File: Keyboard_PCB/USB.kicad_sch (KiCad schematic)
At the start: 3 parts, among them J6 CH_USB_C, U6 USBLC6-2SC6

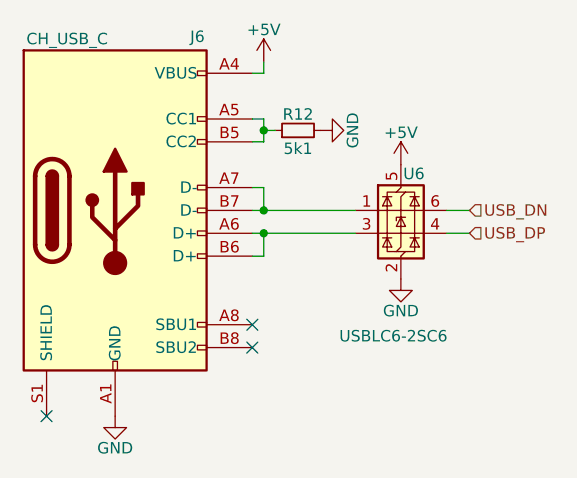
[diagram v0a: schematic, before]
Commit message: STM32U385 pin assignment progress
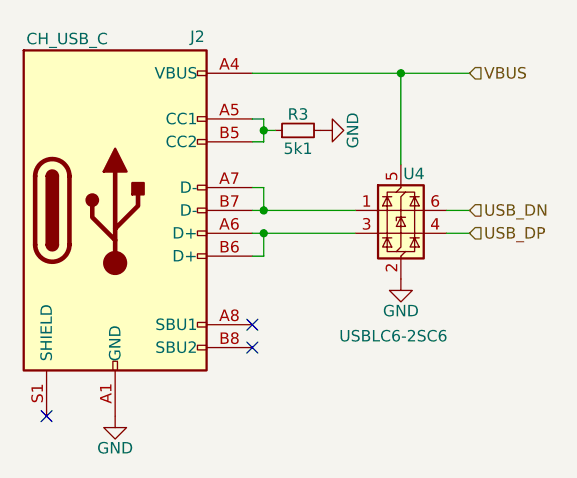
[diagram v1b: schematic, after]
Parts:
- renumbered J6 to J2, R12 to R3, U6 to U4
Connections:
- net +5V renamed VBUS
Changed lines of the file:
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@@
+	)
+	(junction
+		(at 93.98 48.26)
+		(diameter 0)
+		(color 0 0 0 0)
 	)
 	(junction
@@
 	(wire
 		(pts
+			(xy 101.6 48.26) (xy 93.98 48.26)
+		)
+		(stroke
+			(width 0)
+			(type default)
+		)
+	)
+	(wire
+		(pts
 			(xy 78.74 63.5) (xy 77.47 63.5)
 		)
@@
 	(wire
 		(pts
-			(xy 77.47 48.26) (xy 78.74 48.26)
+			(xy 77.47 48.26) (xy 93.98 48.26)
 		)
 		(stroke
@@
 	(wire
 		(pts
-			(xy 78.74 46.99) (xy 78.74 48.26)
-		)
-		(stroke
-			(width 0)
-			(type default)
-		)
-	)
-	(wire
-		(pts
 			(xy 77.47 66.04) (xy 78.74 66.04)
 		)
@@
 		(pts
 			(xy 78.74 66.04) (xy 88.9 66.04)
+		)
+		(stroke
+			(width 0)
+			(type default)
+		)
+	)
+	(wire
+		(pts
+			(xy 93.98 48.26) (xy 93.98 58.42)
 		)
 		(stroke
@@
 		(shape input)
 		(at 101.6 66.04 0)
+		(effects
+			(font
+				(size 1.27 1.27)
+			)
+			(justify left)
+		)
+	)
+	(hierarchical_label "VBUS"
+		(shape input)
+		(at 101.6 48.26 0)
 		(effects
 			(font
@@
 		(on_board yes)
 		(dnp no)
-		(property "Reference" "U6"
+		(property "Reference" "U4"
 			(at 94.234 59.436 0)
 			(effects
@@
 			(project "RF_HID_module_test"
 				(path "/dd51e792-c76c-4d43-96de-494177f3b593/99a36190-5dce-43c5-9e98-275e559646eb"
-					(reference "U6")
+					(reference "U4")
 					(unit 1)
 				)
@@
 		(on_board yes)
 		(dnp no)
-		(property "Reference" "R12"
+		(property "Reference" "R3"
 			(at 82.55 52.832 90)
 			(effects
@@
 			(project ""
 				(path "/dd51e792-c76c-4d43-96de-494177f3b593/99a36190-5dce-43c5-9e98-275e559646eb"
-					(reference "R12")
+					(reference "R3")
 					(unit 1)
 				)
@@
 		(on_board yes)
 		(dnp no)
-		(property "Reference" "#PWR047"
+		(property "Reference" "#PWR014"
 			(at 93.98 77.47 0)
 			(effects
@@
 			(project "RF_HID_module_test"
 				(path "/dd51e792-c76c-4d43-96de-494177f3b593/99a36190-5dce-43c5-9e98-275e559646eb"
-					(reference "#PWR047")
+					(reference "#PWR014")
 					(unit 1)
 				)
@@
 		(on_board yes)
 		(dnp no)
-		(property "Reference" "#PWR045"
+		(property "Reference" "#PWR013"
 			(at 91.44 54.61 0)
 			(effects
@@
 			(project "RF_HID_module_test"
 				(path "/dd51e792-c76c-4d43-96de-494177f3b593/99a36190-5dce-43c5-9e98-275e559646eb"
-					(reference "#PWR045")
-					(unit 1)
-				)
-			)
-		)
-	)
-	(symbol
-		(lib_id "power:+5V")
-		(at 78.74 46.99 0)
-		(unit 1)
-		(exclude_from_sim no)
-		(in_bom yes)
-		(on_board yes)
-		(dnp no)
-		(property "Reference" "#PWR044"
-			(at 78.74 50.8 0)
-			(effects
-				(font
-					(size 1.27 1.27)
-				)
-				(hide yes)
-			)
-		)
-		(property "Value" "+5V"
-			(at 78.74 43.434 0)
-			(effects
-				(font
-					(size 1.27 1.27)
-				)
-			)
-		)
-		(property "Footprint" ""
-			(at 78.74 46.99 0)
-			(effects
-				(font
-					(size 1.27 1.27)
-				)
-				(hide yes)
-			)
-		)
-		(property "Datasheet" ""
-			(at 78.74 46.99 0)
-			(effects
-				(font
-					(size 1.27 1.27)
-				)
-				(hide yes)
-			)
-		)
-		(property "Description" "Power symbol creates a global label with name \"+5V\""
-			(at 78.74 46.99 0)
-			(effects
-				(font
-					(size 1.27 1.27)
-				)
-				(hide yes)
-			)
-		)
-		(pin "1"
-		)
-		(instances
-			(project "RF_HID_module_test"
-				(path "/32b1f824-104d-4f37-b265-1c31215c2fe4/3052776d-f0df-4f5c-b23a-46f73ae78b94"
-					(reference "#PWR044")
-					(unit 1)
-				)
-				(path "/32b1f824-104d-4f37-b265-1c31215c2fe4/35fb170e-cc4d-4774-8b9f-87fa9e2bb590"
-					(reference "#PWR049")
-					(unit 1)
-				)
-			)
-			(project "RF_HID_module_test"
-				(path "/dd51e792-c76c-4d43-96de-494177f3b593/99a36190-5dce-43c5-9e98-275e559646eb"
-					(reference "#PWR044")
+					(reference "#PWR013")
 					(unit 1)
 				)
@@
 		(on_board yes)
 		(dnp no)
-		(property "Reference" "#PWR048"
+		(property "Reference" "#PWR015"
 			(at 62.23 92.71 0)
 			(effects
@@
 			(project "RF_HID_module_test"
 				(path "/dd51e792-c76c-4d43-96de-494177f3b593/99a36190-5dce-43c5-9e98-275e559646eb"
-					(reference "#PWR048")
-					(unit 1)
-				)
-			)
-		)
-	)
-	(symbol
-		(lib_id "power:+5V")
-		(at 93.98 58.42 0)
-		(unit 1)
-		(exclude_from_sim no)
-		(in_bom yes)
-		(on_board yes)
-		(dnp no)
-		(property "Reference" "#PWR046"
-			(at 93.98 62.23 0)
-			(effects
-				(font
-					(size 1.27 1.27)
-				)
-				(hide yes)
-			)
-		)
-		(property "Value" "+5V"
-			(at 93.98 54.864 0)
-			(effects
-				(font
-					(size 1.27 1.27)
-				)
-			)
-		)
-		(property "Footprint" ""
-			(at 93.98 58.42 0)
-			(effects
-				(font
-					(size 1.27 1.27)
-				)
-				(hide yes)
-			)
-		)
-		(property "Datasheet" ""
-			(at 93.98 58.42 0)
-			(effects
-				(font
-					(size 1.27 1.27)
-				)
-				(hide yes)
-			)
-		)
-		(property "Description" "Power symbol creates a global label with name \"+5V\""
-			(at 93.98 58.42 0)
-			(effects
-				(font
-					(size 1.27 1.27)
-				)
-				(hide yes)
-			)
-		)
-		(pin "1"
-		)
-		(instances
-			(project "RF_HID_module_test"
-				(path "/32b1f824-104d-4f37-b265-1c31215c2fe4/3052776d-f0df-4f5c-b23a-46f73ae78b94"
-					(reference "#PWR046")
-					(unit 1)
-				)
-				(path "/32b1f824-104d-4f37-b265-1c31215c2fe4/35fb170e-cc4d-4774-8b9f-87fa9e2bb590"
-					(reference "#PWR051")
-					(unit 1)
-				)
-			)
-			(project "RF_HID_module_test"
-				(path "/dd51e792-c76c-4d43-96de-494177f3b593/99a36190-5dce-43c5-9e98-275e559646eb"
-					(reference "#PWR046")
+					(reference "#PWR015")
 					(unit 1)
 				)
@@
 		(on_board yes)
 		(dnp no)
-		(property "Reference" "J6"
+		(property "Reference" "J2"
 			(at 71.374 44.196 0)
 			(effects
@@
 			(project "RF_HID_module_test"
 				(path "/dd51e792-c76c-4d43-96de-494177f3b593/99a36190-5dce-43c5-9e98-275e559646eb"
-					(reference "J6")
-					(unit 1)
-				)
+					(reference "J2")
+					(unit 1)
+				)

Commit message: Schematic done
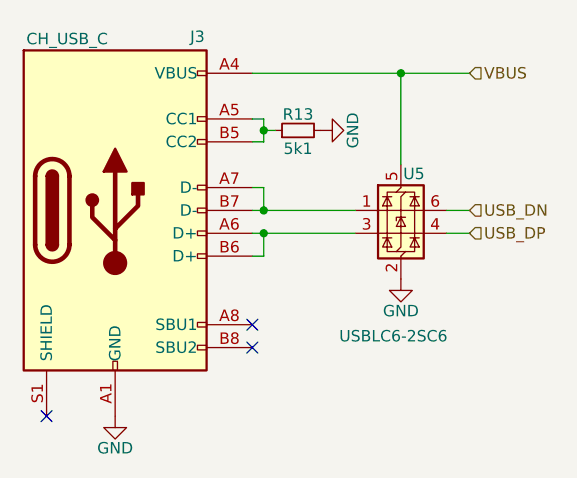
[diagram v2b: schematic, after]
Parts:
- renumbered J2 to J3, R3 to R13, U4 to U5
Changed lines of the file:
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@@
 		(on_board yes)
 		(dnp no)
-		(property "Reference" "U4"
+		(property "Reference" "U5"
 			(at 94.234 59.436 0)
 			(effects
@@
 			(project "RF_HID_module_test"
 				(path "/dd51e792-c76c-4d43-96de-494177f3b593/99a36190-5dce-43c5-9e98-275e559646eb"
-					(reference "U4")
+					(reference "U5")
 					(unit 1)
 				)
@@
 		(on_board yes)
 		(dnp no)
-		(property "Reference" "R3"
+		(property "Reference" "R13"
 			(at 82.55 52.832 90)
 			(effects
@@
 			(project ""
 				(path "/dd51e792-c76c-4d43-96de-494177f3b593/99a36190-5dce-43c5-9e98-275e559646eb"
-					(reference "R3")
+					(reference "R13")
 					(unit 1)
 				)
@@
 		(on_board yes)
 		(dnp no)
-		(property "Reference" "#PWR014"
+		(property "Reference" "#PWR059"
 			(at 93.98 77.47 0)
 			(effects
@@
 			(project "RF_HID_module_test"
 				(path "/dd51e792-c76c-4d43-96de-494177f3b593/99a36190-5dce-43c5-9e98-275e559646eb"
-					(reference "#PWR014")
+					(reference "#PWR059")
 					(unit 1)
 				)
@@
 		(on_board yes)
 		(dnp no)
-		(property "Reference" "#PWR013"
+		(property "Reference" "#PWR058"
 			(at 91.44 54.61 0)
 			(effects
@@
 			(project "RF_HID_module_test"
 				(path "/dd51e792-c76c-4d43-96de-494177f3b593/99a36190-5dce-43c5-9e98-275e559646eb"
-					(reference "#PWR013")
+					(reference "#PWR058")
 					(unit 1)
 				)
@@
 		(on_board yes)
 		(dnp no)
-		(property "Reference" "#PWR015"
+		(property "Reference" "#PWR060"
 			(at 62.23 92.71 0)
 			(effects
@@
 			(project "RF_HID_module_test"
 				(path "/dd51e792-c76c-4d43-96de-494177f3b593/99a36190-5dce-43c5-9e98-275e559646eb"
-					(reference "#PWR015")
+					(reference "#PWR060")
 					(unit 1)
 				)
@@
 		(on_board yes)
 		(dnp no)
-		(property "Reference" "J2"
+		(property "Reference" "J3"
 			(at 71.374 44.196 0)
 			(effects
@@
 			(project "RF_HID_module_test"
 				(path "/dd51e792-c76c-4d43-96de-494177f3b593/99a36190-5dce-43c5-9e98-275e559646eb"
-					(reference "J2")
-					(unit 1)
-				)
+					(reference "J3")
+					(unit 1)
+				)

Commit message: eMMC routing and STM passives
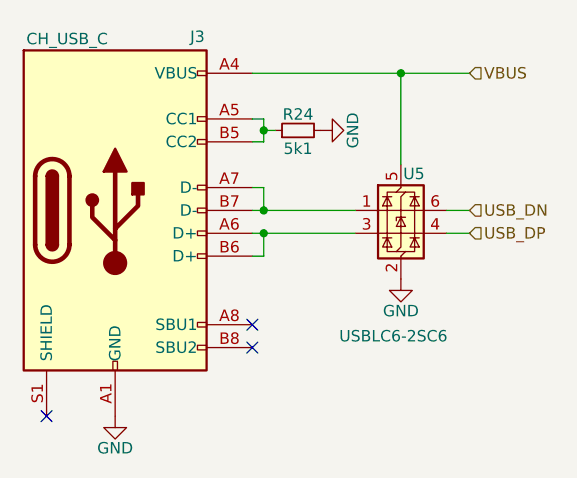
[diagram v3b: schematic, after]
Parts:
- renumbered R13 to R24
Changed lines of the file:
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@@
 		(on_board yes)
 		(dnp no)
-		(property "Reference" "R13"
+		(property "Reference" "R24"
 			(at 82.55 52.832 90)
 			(effects
@@
 			(project ""
 				(path "/dd51e792-c76c-4d43-96de-494177f3b593/99a36190-5dce-43c5-9e98-275e559646eb"
-					(reference "R13")
+					(reference "R24")
 					(unit 1)
 				)
@@
 		(on_board yes)
 		(dnp no)
-		(property "Reference" "#PWR059"
+		(property "Reference" "#PWR072"
 			(at 93.98 77.47 0)
 			(effects
@@
 			(project "RF_HID_module_test"
 				(path "/dd51e792-c76c-4d43-96de-494177f3b593/99a36190-5dce-43c5-9e98-275e559646eb"
-					(reference "#PWR059")
+					(reference "#PWR072")
 					(unit 1)
 				)
@@
 		(on_board yes)
 		(dnp no)
-		(property "Reference" "#PWR058"
+		(property "Reference" "#PWR071"
 			(at 91.44 54.61 0)
 			(effects
@@
 			(project "RF_HID_module_test"
 				(path "/dd51e792-c76c-4d43-96de-494177f3b593/99a36190-5dce-43c5-9e98-275e559646eb"
-					(reference "#PWR058")
+					(reference "#PWR071")
 					(unit 1)
 				)
@@
 		(on_board yes)
 		(dnp no)
-		(property "Reference" "#PWR060"
+		(property "Reference" "#PWR073"
 			(at 62.23 92.71 0)
 			(effects
@@
 			(project "RF_HID_module_test"
 				(path "/dd51e792-c76c-4d43-96de-494177f3b593/99a36190-5dce-43c5-9e98-275e559646eb"
-					(reference "#PWR060")
-					(unit 1)
-				)
+					(reference "#PWR073")
+					(unit 1)
+				)

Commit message: Added mouser IDs to components and checked STM-eMMC connection
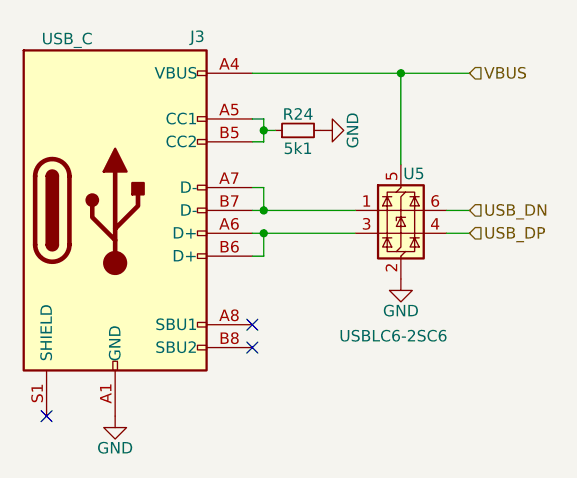
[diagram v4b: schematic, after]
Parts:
- J3: value CH_USB_C -> USB_C; now left out of the parts list
- R24, U5: now left out of the parts list
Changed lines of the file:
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@@
 		(unit 1)
 		(exclude_from_sim no)
-		(in_bom yes)
+		(in_bom no)
 		(on_board yes)
 		(dnp no)
@@
 		)
 		(property "LCSC" "C2827654"
+			(at 93.98 63.5 0)
+			(effects
+				(font
+					(size 1.27 1.27)
+				)
+				(hide yes)
+			)
+		)
+		(property "aliexpress" ""
 			(at 93.98 63.5 0)
 			(effects
@@
 		(unit 1)
 		(exclude_from_sim no)
-		(in_bom yes)
+		(in_bom no)
 		(on_board yes)
 		(dnp no)
@@
 		(property "Description" "Resistor, small symbol"
 			(at 82.55 54.61 0)
+			(effects
+				(font
+					(size 1.27 1.27)
+				)
+				(hide yes)
+			)
+		)
+		(property "aliexpress" ""
+			(at 82.55 54.61 90)
 			(effects
 				(font
@@
 		(unit 1)
 		(exclude_from_sim no)
-		(in_bom yes)
+		(in_bom no)
 		(on_board yes)
 		(dnp no)
@@
 			)
 		)
-		(property "Value" "CH_USB_C"
+		(property "Value" "USB_C"
 			(at 56.896 44.45 0)
 			(effects
@@
 			(at 62.23 63.5 0)
 			(effects
+				(font
+					(size 1.27 1.27)
+				)
+				(hide yes)
+			)
+		)
+		(property "aliexpress" ""
+			(at 62.23 63.5 0)
+			(effects

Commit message: Improved battery sens and added JLCPCB QR code
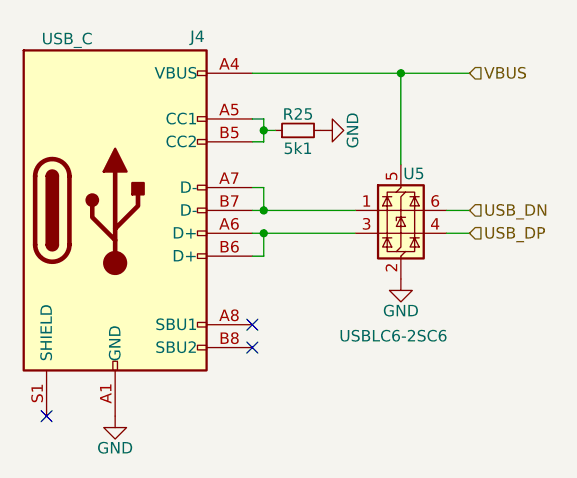
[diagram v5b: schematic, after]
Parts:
- renumbered J3 to J4, R24 to R25
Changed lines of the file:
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@@
 		(on_board yes)
 		(dnp no)
-		(property "Reference" "R24"
+		(property "Reference" "R25"
 			(at 82.55 52.832 90)
 			(effects
@@
 			(project ""
 				(path "/dd51e792-c76c-4d43-96de-494177f3b593/99a36190-5dce-43c5-9e98-275e559646eb"
-					(reference "R24")
+					(reference "R25")
 					(unit 1)
 				)
@@
 		(on_board yes)
 		(dnp no)
-		(property "Reference" "#PWR072"
+		(property "Reference" "#PWR074"
 			(at 93.98 77.47 0)
 			(effects
@@
 			(project "RF_HID_module_test"
 				(path "/dd51e792-c76c-4d43-96de-494177f3b593/99a36190-5dce-43c5-9e98-275e559646eb"
-					(reference "#PWR072")
+					(reference "#PWR074")
 					(unit 1)
 				)
@@
 		(on_board yes)
 		(dnp no)
-		(property "Reference" "#PWR071"
+		(property "Reference" "#PWR073"
 			(at 91.44 54.61 0)
 			(effects
@@
 			(project "RF_HID_module_test"
 				(path "/dd51e792-c76c-4d43-96de-494177f3b593/99a36190-5dce-43c5-9e98-275e559646eb"
-					(reference "#PWR071")
+					(reference "#PWR073")
 					(unit 1)
 				)
@@
 		(on_board yes)
 		(dnp no)
-		(property "Reference" "#PWR073"
+		(property "Reference" "#PWR075"
 			(at 62.23 92.71 0)
 			(effects
@@
 			(project "RF_HID_module_test"
 				(path "/dd51e792-c76c-4d43-96de-494177f3b593/99a36190-5dce-43c5-9e98-275e559646eb"
-					(reference "#PWR073")
+					(reference "#PWR075")
 					(unit 1)
 				)
@@
 		(on_board yes)
 		(dnp no)
-		(property "Reference" "J3"
+		(property "Reference" "J4"
 			(at 71.374 44.196 0)
 			(effects
@@
 			(project "RF_HID_module_test"
 				(path "/dd51e792-c76c-4d43-96de-494177f3b593/99a36190-5dce-43c5-9e98-275e559646eb"
-					(reference "J3")
-					(unit 1)
-				)
+					(reference "J4")
+					(unit 1)
+				)

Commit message: Added active battery sensing circuit
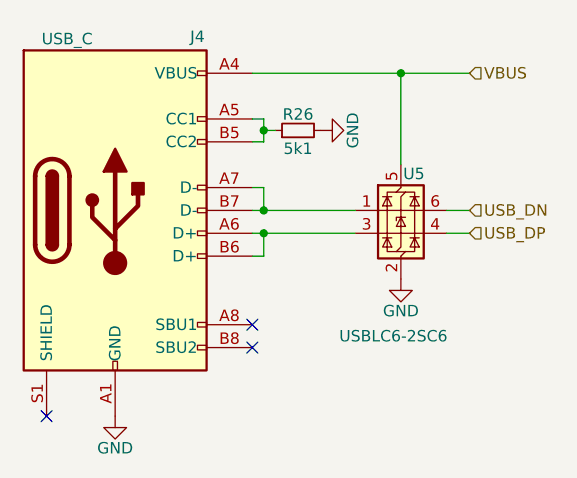
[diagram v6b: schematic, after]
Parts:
- renumbered R25 to R26
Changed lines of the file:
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@@
 		(on_board yes)
 		(dnp no)
-		(property "Reference" "R25"
+		(property "Reference" "R26"
 			(at 82.55 52.832 90)
 			(effects
@@
 			(project ""
 				(path "/dd51e792-c76c-4d43-96de-494177f3b593/99a36190-5dce-43c5-9e98-275e559646eb"
-					(reference "R25")
+					(reference "R26")
 					(unit 1)
 				)
